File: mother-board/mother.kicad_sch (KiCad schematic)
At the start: 32 parts, among them J1 Screw_Terminal_01x02, J10 Conn_02x03_Odd_Even, J11 Screw_Terminal_01x02, J12 Screw_Terminal_01x02, J2 Screw_Terminal_01x02, J3 Screw_Terminal_01x02, J4 Screw_Terminal_01x02, J5 Screw_Terminal_01x02, J6 Screw_Terminal_01x02, J7 Screw_Terminal_01x02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

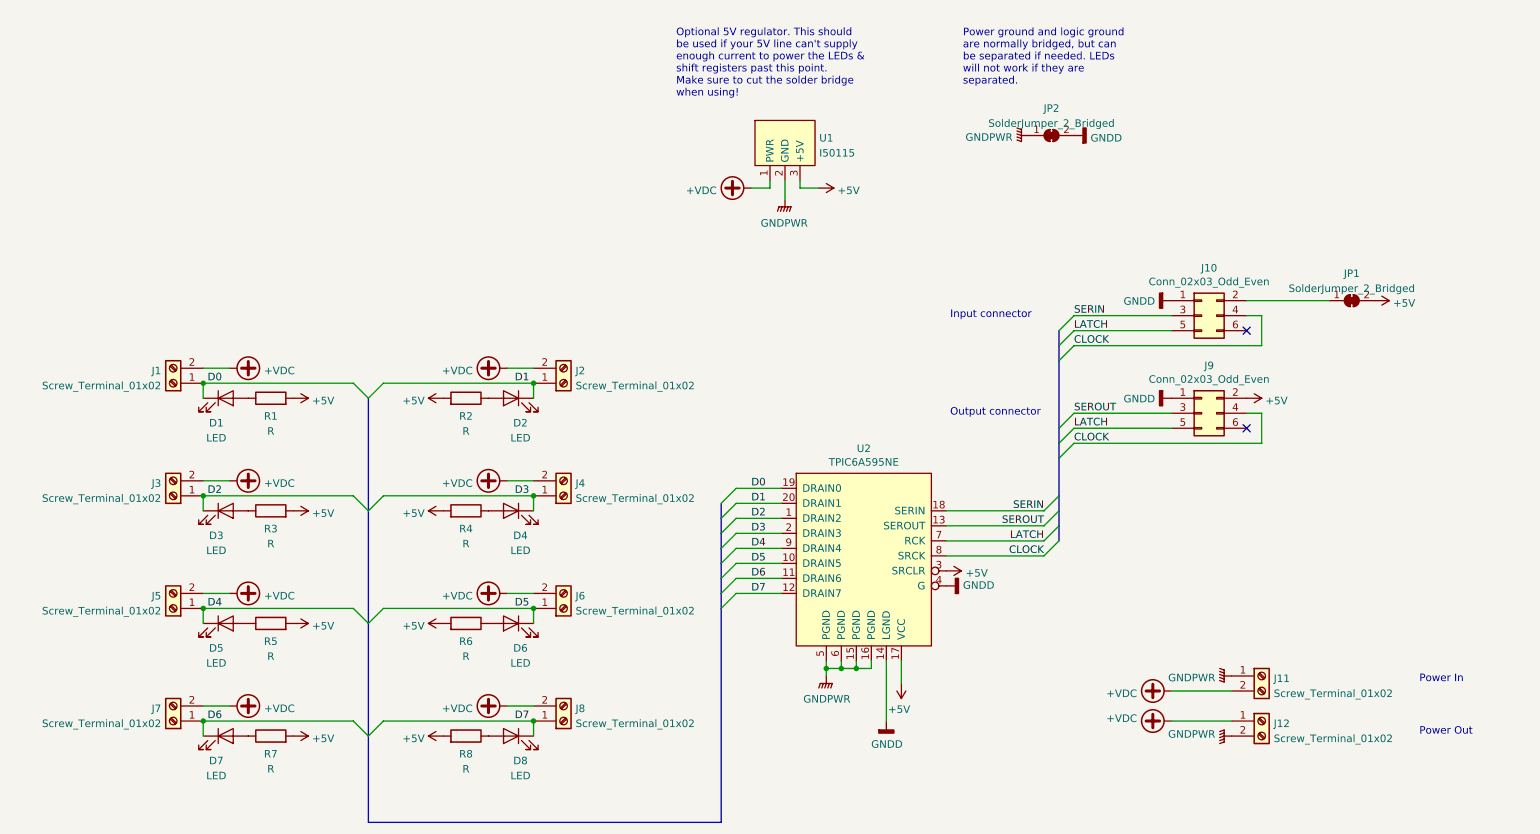
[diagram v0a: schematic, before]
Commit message: add rev 0 boards
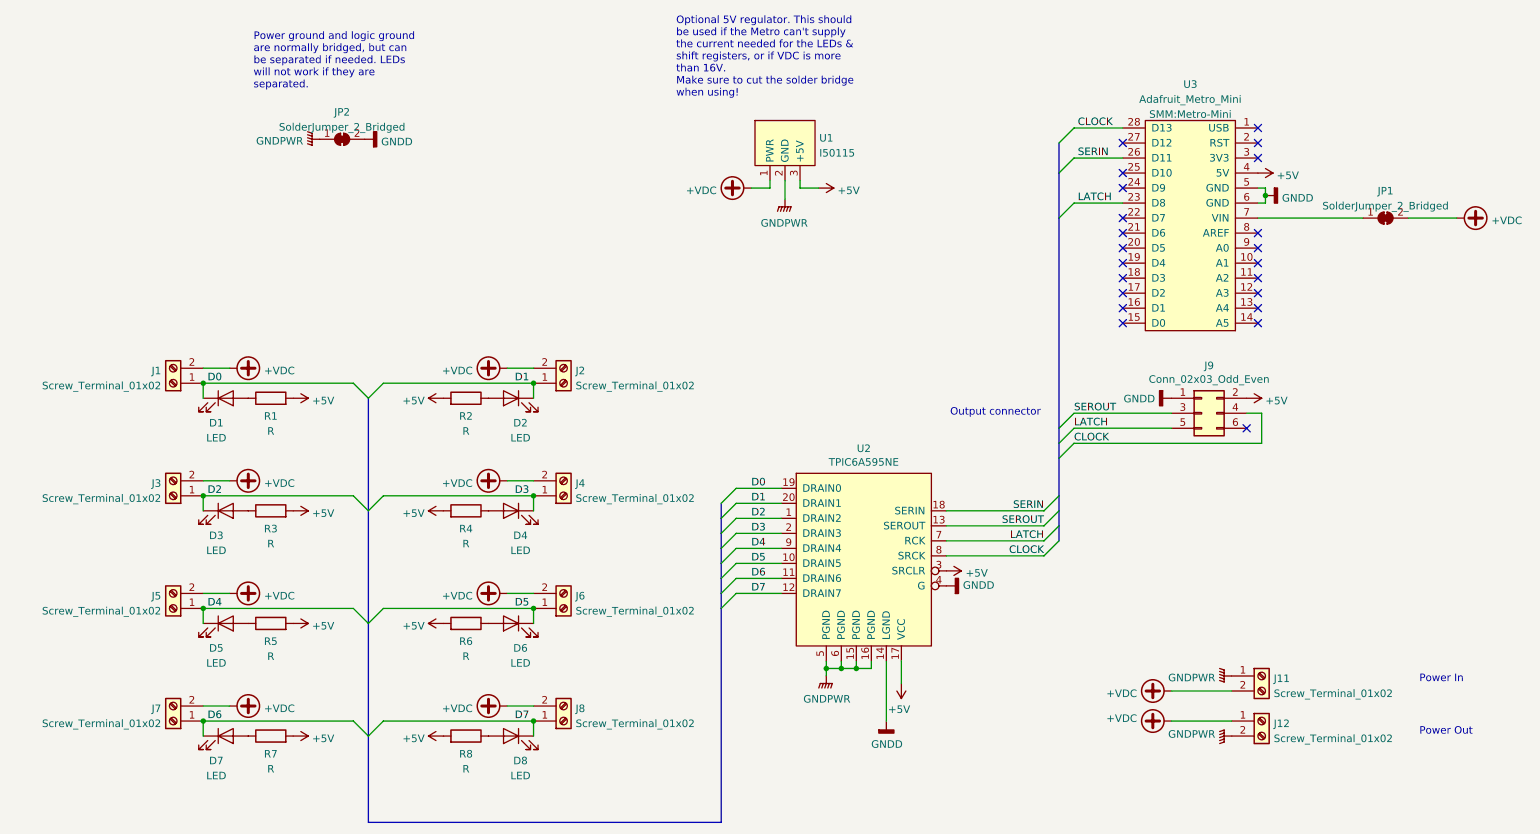
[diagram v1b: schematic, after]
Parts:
- removed J10: Conn_02x03_Odd_Even, Connector_IDC:IDC-Header_2x03_P2.54mm_Vertical, symbol Connector_Generic:Conn_02x03_Odd_Even
- added U3: Adafruit_Metro_Mini, SMM:Metro-Mini, symbol SMM:Adafruit_Metro_Mini
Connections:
- net +5V: now also U3.4 (5V); no longer JP1.2 (B)
- net +VDC: now also JP1.2 (B)
- net CLOCK: now also U3.28 (D13)
- net GNDD: now also U3.5 (GND), U3.6 (GND)
- net LATCH: now also U3.23 (D8)
- net SERIN: now also U3.26 (D11)
- net at JP1.1 (A): now also U3.7 (VIN)
- no-connect marks 2 -> 22
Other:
- note added: "Optional 5V regulator. This should be used if the Metro can't supply the current needed for the LEDs & shift registers, or if VDC is more than 16V. Make sure to cut the solder bridge when using!"
- note removed: "Input connector"
- note removed: "Optional 5V regulator. This should be used if your 5V line can't supply enough current to power the LEDs & shift registers past this point. Make sure to cut the solder bridge when using!"
- moved on the sheet: JP2
